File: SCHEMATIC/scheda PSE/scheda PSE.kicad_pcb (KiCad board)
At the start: 2 copper layers, 102.4 x 77.4 mm, 124 parts, among them J1 Debug, J2 Vin, J3 USB_B_Mini, J4 Vout 5V, J5 I2C_3V3, J6 UART0_3V3, Q1 IRLML0060TRPBF, Q2 PDTC114YT, Q3 IRLML9301, SW1 RESET_SW, SW2 PROG_SW, SW3 SW_U, SW4 SW_L, SW5 SW_R, SW6 SW_D, SW7 Power_button, U1 RP2040, U2 W25Q16JVUSSQ, U3 AT24C256, U4 oled_0.96"_128x64px, U5 TPS563201, U6 XC6705A331MR-G, U7 SAM-M8Q, U8 MMA8451Q, U9 TC1047A, Y1 12MHz

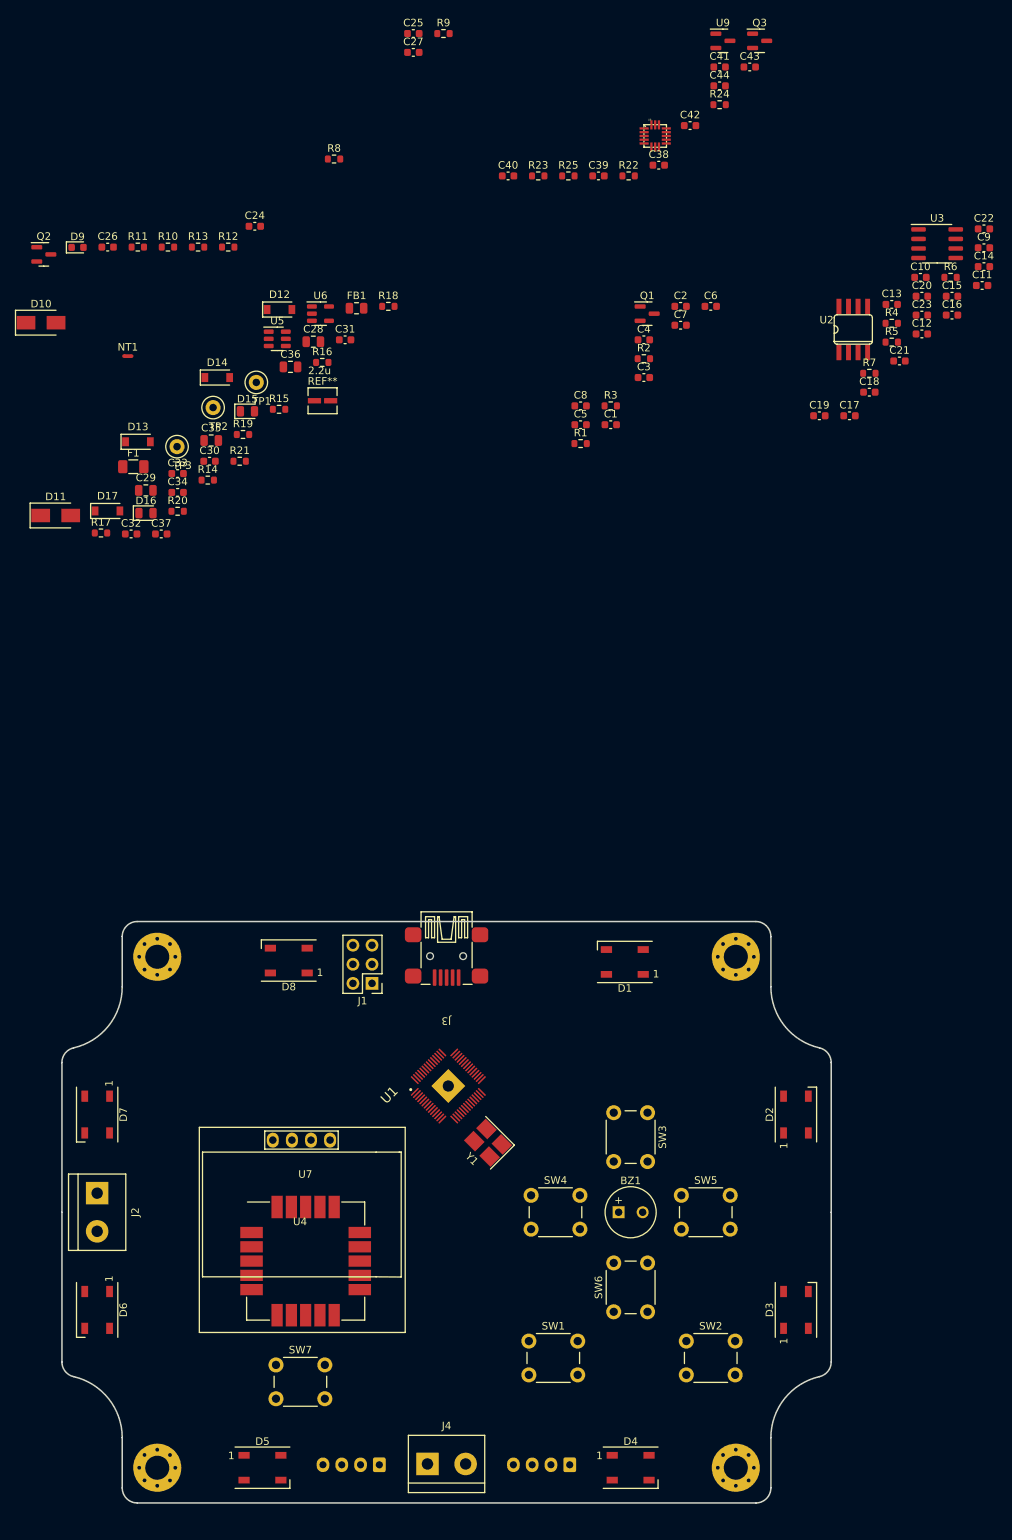
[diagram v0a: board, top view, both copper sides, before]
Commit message: Posizionati tutti i componenti
Posizionati tutti i componenti sulla scheda
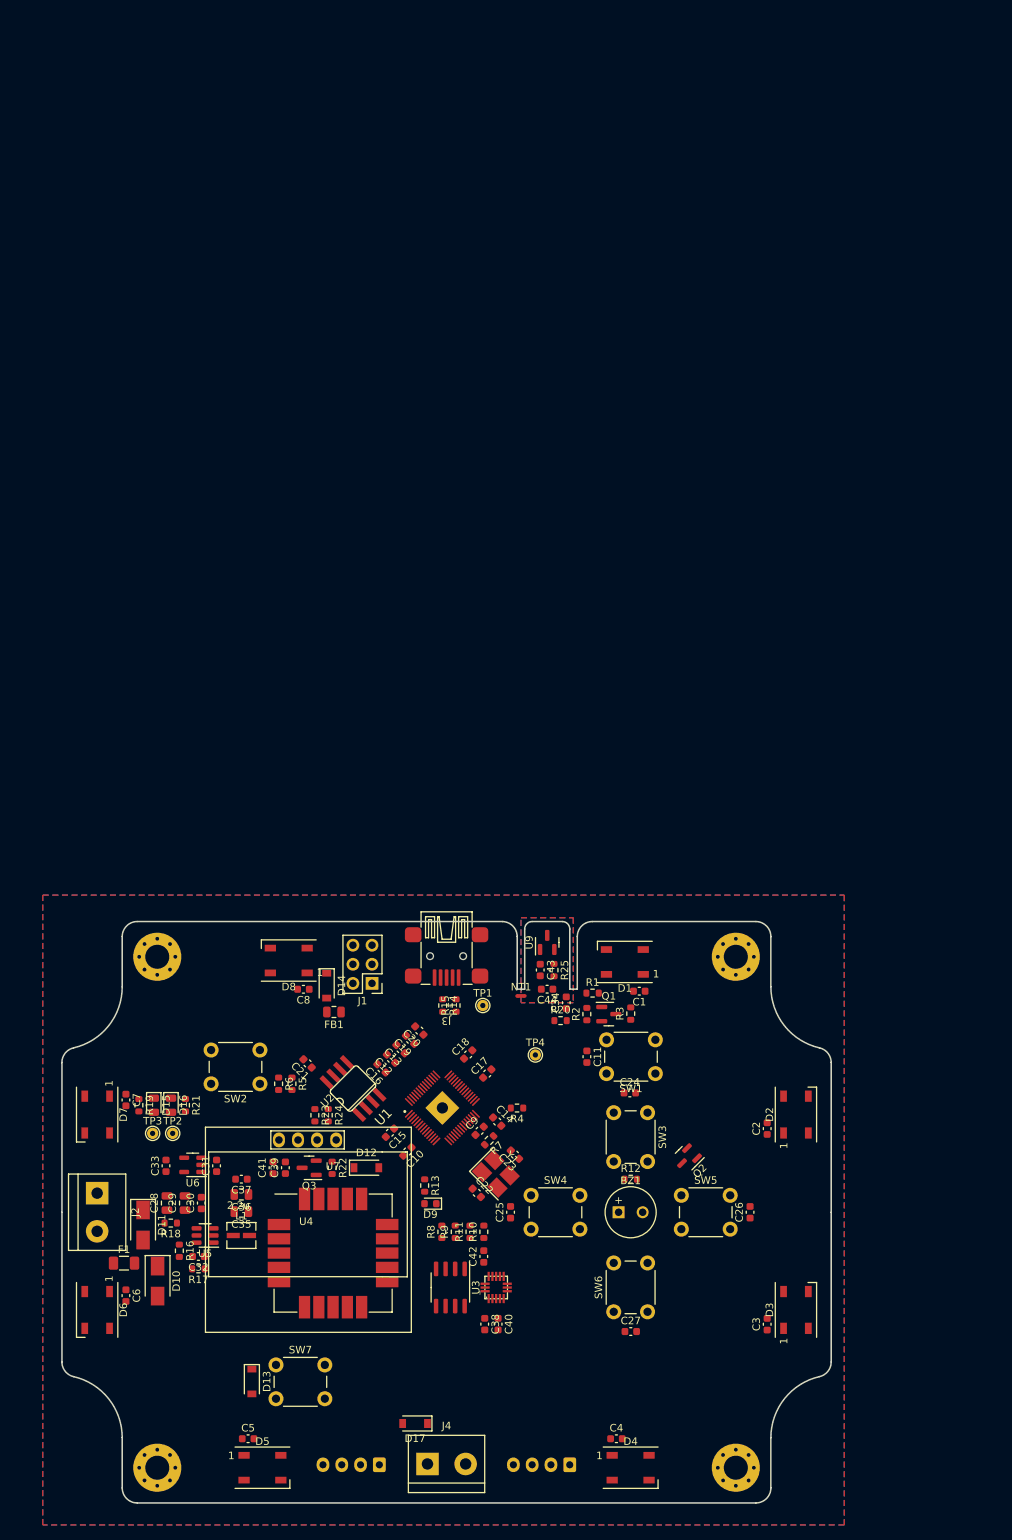
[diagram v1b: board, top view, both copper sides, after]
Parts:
- added TP2: 5V, TestPoint:TestPoint_THTPad_D1.5mm_Drill0.7mm, F.Cu at (119.1, 86.5)
- TP1: footprint TestPoint:TestPoint_Loop_D2.50mm_Drill1.0mm_LowProfile -> TestPoint:TestPoint_THTPad_D1.5mm_Drill0.7mm
- TP3: renamed from TP2; footprint TestPoint:TestPoint_Loop_D2.50mm_Drill1.0mm_LowProfile -> TestPoint:TestPoint_THTPad_D1.5mm_Drill0.7mm
- TP4: renamed from TP3; footprint TestPoint:TestPoint_Loop_D2.50mm_Drill1.0mm_LowProfile -> TestPoint:TestPoint_THTPad_D1.5mm_Drill0.7mm
- moved C27 172.7 mm to (180.0, 112.9)
- moved Q3 161.5 mm to (137.2, 91.1), turned to 180 degrees
- moved R9 159.5 mm to (156.7, 99.6), turned to 90 degrees
- moved C41 158.1 mm to (132.4, 91.1), turned to 90 degrees
- moved C25 157.4 mm to (164.0, 97.0), turned to 90 degrees
- moved C38 156.0 mm to (160.6, 111.9), turned to -90 degrees
- moved U8 154.7 mm to (162.1, 107.0), turned to 90 degrees
- moved C26 154.3 mm to (195.9, 97.0), turned to 90 degrees
- moved U3 153.3 mm to (156.0, 107.0), turned to -90 degrees
- moved C42 153.0 mm to (160.5, 102.9), turned to 90 degrees
- moved C6 152.9 mm to (112.8, 108.1), turned to -90 degrees
- moved C40 152.8 mm to (162.4, 111.9), turned to -90 degrees
- moved Q2 147.6 mm to (187.5, 89.8), turned to -135 degrees
- moved C4 146.3 mm to (178.1, 127.1)
- moved C22 145.0 mm to (159.5, 94.4), turned to -45 degrees
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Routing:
- added copper zone on B.Cu, net GND
- added copper zone on F.Cu, net GND
- added copper zone on B.Cu, net GNDA
- added copper zone on F.Cu, net GNDA
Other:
- outline, holes or cut-outs redrawn

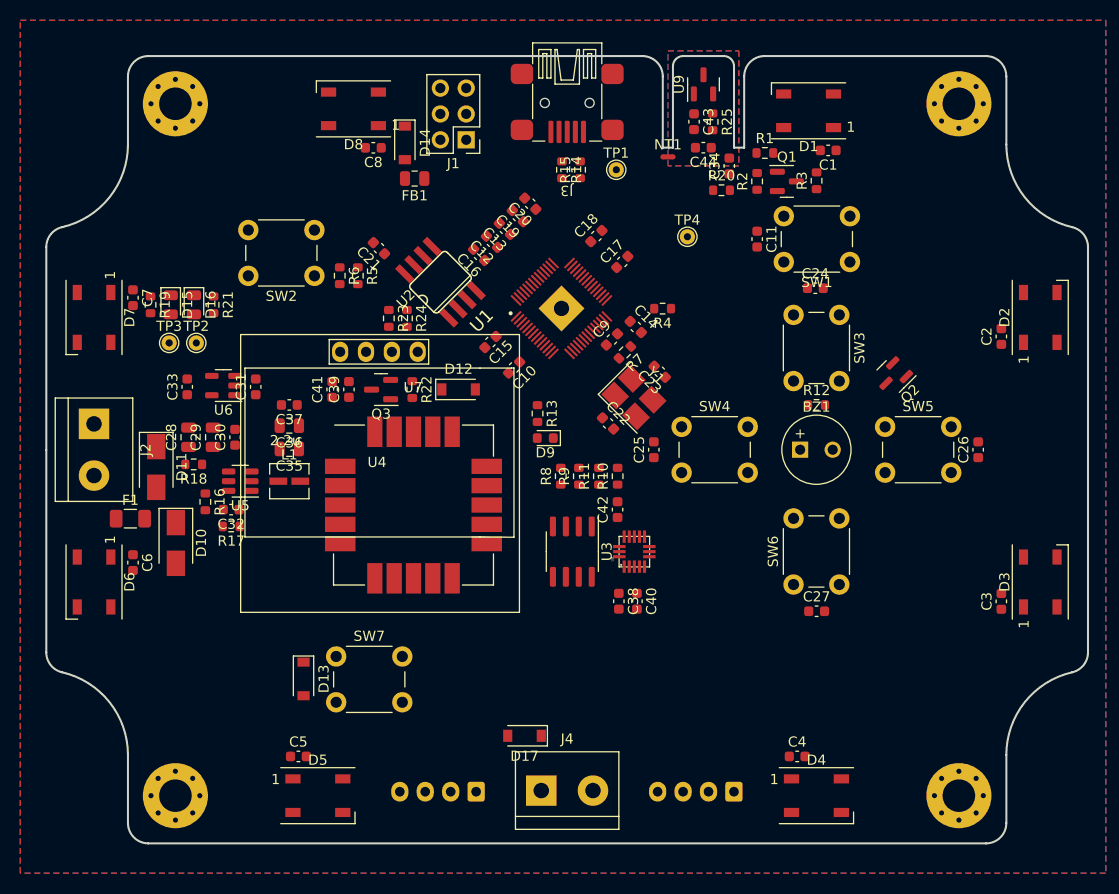
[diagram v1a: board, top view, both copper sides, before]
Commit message: iniziato lo broglio. Prima di continuare modificare pin schema
iniziato lo sbroglio della scheda, prima di continuare bisogna sistemare i pin che siano concordi con quelli degli altro (ovvero sistemarli come da tabella su telegram)
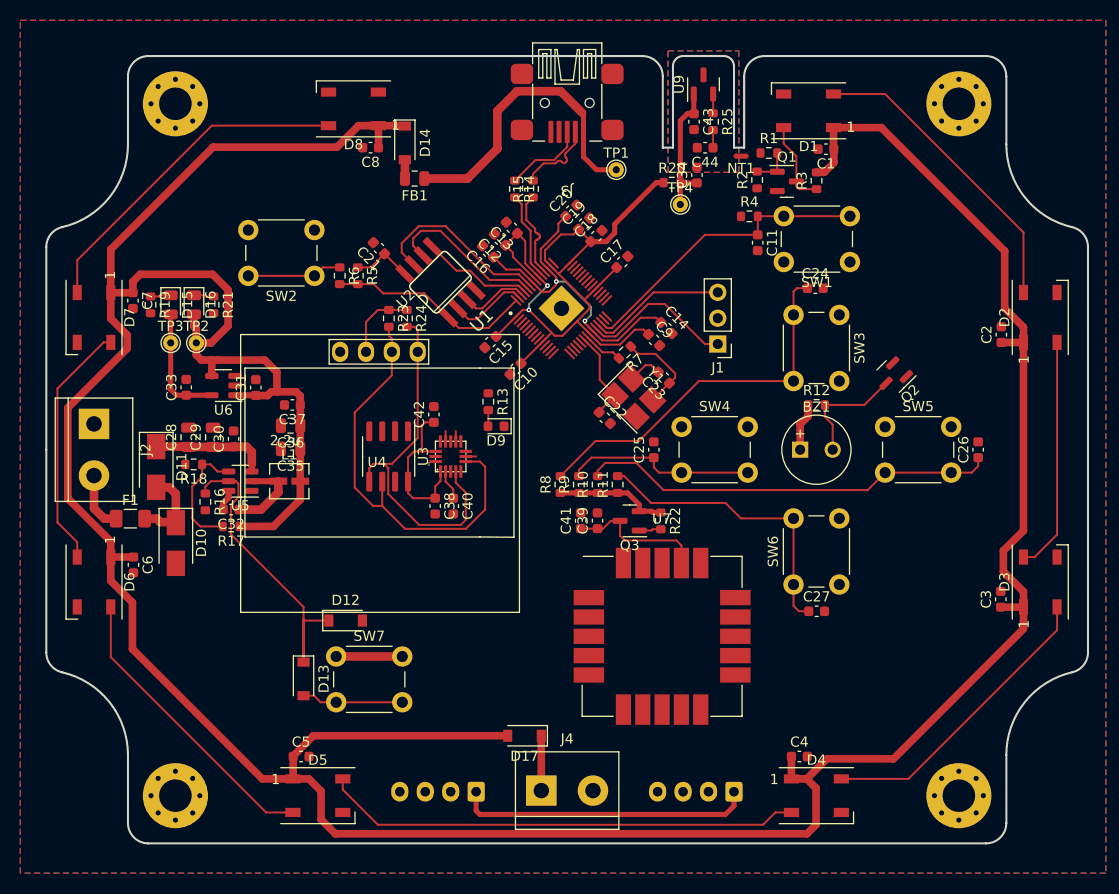
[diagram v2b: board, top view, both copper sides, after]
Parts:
- J1: value Debug -> Conn_01x03; footprint Connector_PinHeader_2.54mm:PinHeader_2x03_P2.54mm_Vertical -> Connector_PinHeader_2.54mm:PinHeader_1x03_P2.54mm_Vertical
- moved J1 31.8 mm to (170.3, 86.6)
- moved U7 27.6 mm to (165.1, 115.3)
- moved C41 27.6 mm to (156.8, 104.0)
- moved Q3 27.6 mm to (161.6, 104.0)
- moved R22 27.6 mm to (164.7, 104.0)
- moved C39 27.6 mm to (158.5, 104.0)
- moved D12 25.3 mm to (133.7, 113.8)
- moved C40 20.3 mm to (144.3, 102.5)
- moved C42 20.3 mm to (142.4, 93.5)
- moved C38 20.3 mm to (142.5, 102.5)
- moved U3 20.3 mm to (138.0, 97.7)
- moved U8 20.3 mm to (144.1, 97.7)
- moved R4 12.5 mm to (173.4, 74.1), turned to 0 degrees
- moved NT1 7.19 mm to (172.6, 68.1), turned to 180 degrees
- moved C19 6.56 mm to (157.2, 74.8), turned to 45 degrees
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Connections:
- net Net-(J3-Pad2) renamed /Alimentazione/D-
- net Net-(J3-Pad3) renamed /Alimentazione/D+
- C43 pad 1: +3V3 -> +3.3VA
- J1 pad 1: +3V3 -> /RP2040/SWCLK
- J1 pad 3: /RP2040/I2C1_SDA -> /RP2040/SWDIO
- J5 pad 1: +3.3V -> +3V3
- J6 pad 1: +3.3V -> +3V3
- R15 pad 1: /Alimentazione/USB_DM -> /Alimentazione/USB_DN
- U1 pad 29: /RP2040/I2C1_SDA -> unconnected-(U1-Pad29)
- U1 pad 30: /RP2040/I2C1_SCL -> unconnected-(U1-Pad30)
- U1 pad 46: /Alimentazione/USB_DP -> /Alimentazione/USB_DN
- U1 pad 47: /Alimentazione/USB_DM -> /Alimentazione/USB_DP
- U1 pad 54: /RP2040/FLASH_D2 -> /RP2040/~{FLASH_D2}
- U3 pad 8: +3.3V -> +3V3
- U9 pad 1: +3V3 -> +3.3VA
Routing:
- net +5V: track 0.00 -> 357.5 mm
- net +3V3: track 0.00 -> 155.1 mm, vias 0 -> 2
- net Net-(D4-Pad2): track 0.00 -> 47.1 mm
- net /I2C0_SCL: track 0.00 -> 41.4 mm
- net /Interfaccia utente/BUTTON_R: track 0.00 -> 41.2 mm
- net /Interfaccia utente/BUTTON_U: track 0.00 -> 37.1 mm
- net /I2C0_SDA: track 0.00 -> 36.8 mm
- net Net-(D7-Pad2): track 0.00 -> 33.4 mm
- net +1V1: track 0.00 -> 31.8 mm, vias 0 -> 2
- net /Alimentazione/BUCK_EN: track 0.00 -> 31.8 mm
- net /RP2040/RUN: track 0.00 -> 30.3 mm
- net /Alimentazione/VBUS: track 0.00 -> 30.2 mm
- net Net-(D1-Pad2): track 0.00 -> 30.2 mm
- net Net-(D3-Pad2): track 0.00 -> 29.5 mm
- net /Interfaccia utente/BUTTON_D: track 0.00 -> 29.3 mm
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
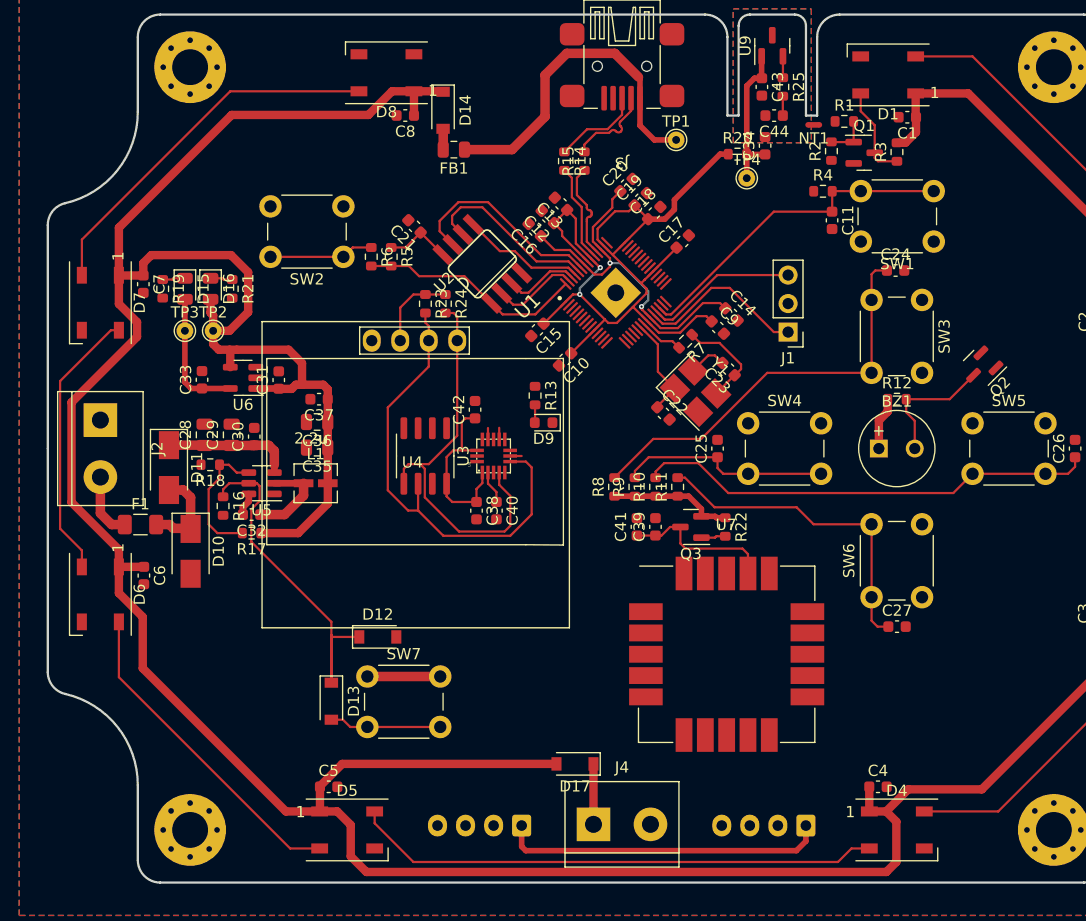
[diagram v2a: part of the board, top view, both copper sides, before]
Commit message: sistemato buzzer, e continuato lo sbroglio
sistemato il buzzer con un altro footprint e ho continuato lo sbroglio.
Teoricamente manca solo collegare i collegamenti tra le gpio del rp2040 e il resto dei componenti
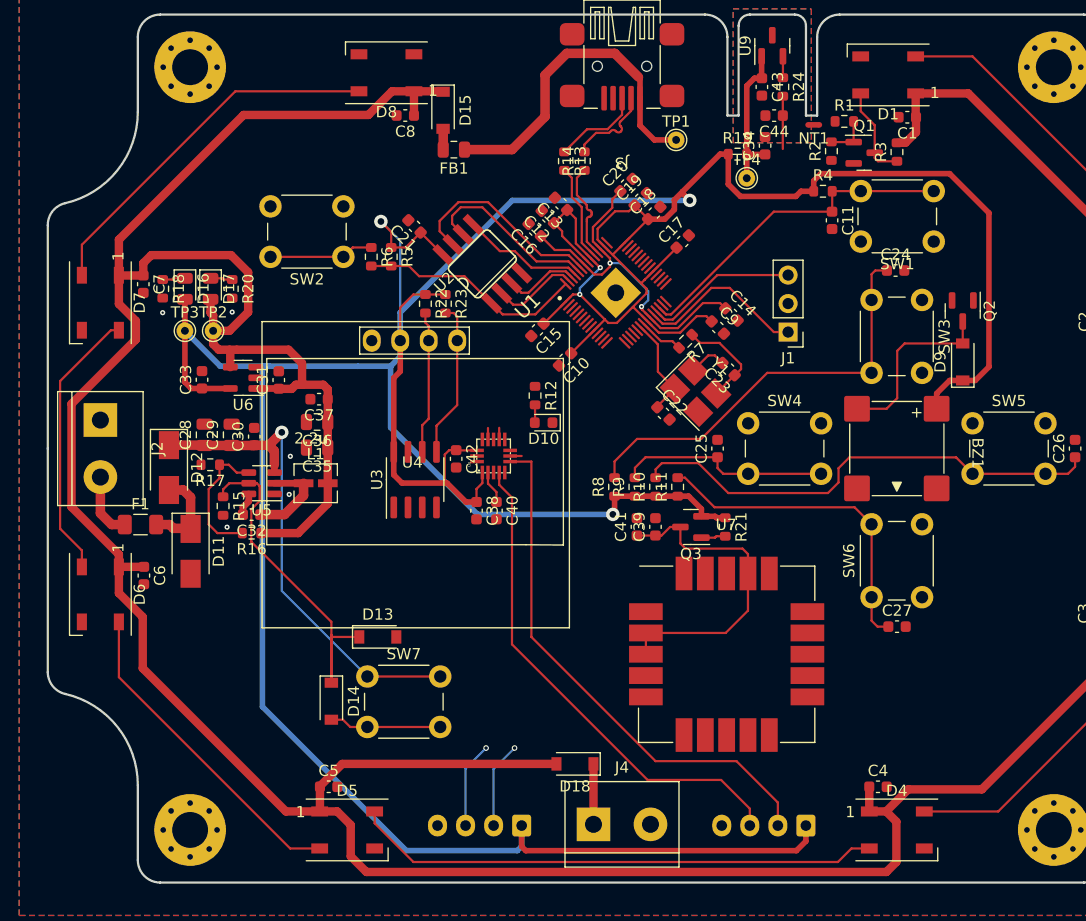
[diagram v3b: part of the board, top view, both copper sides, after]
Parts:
- removed the R12 at (180.0, 92.6)
- added D9: 1N4148, Diode_SMD:D_SOD-123, F.Cu at (185.9, 89.3)
- BZ1: footprint Buzzer_Beeper:MagneticBuzzer_Kingstate_KCG0601 -> _PSE:MLT-8530
- moved Q2 5.33 mm to (185.9, 84.7), turned to -90 degrees
- moved C42 4.70 mm to (140.7, 97.9), turned to -90 degrees
- moved U3 2.29 mm to (137.1, 99.8), turned to 90 degrees
- moved BZ1 1.60 mm to (180.0, 97.0), turned to -90 degrees
- renumbered D9 to D10, D10 to D11, D11 to D12, D12 to D13, D13 to D14, D14 to D15, D15 to D16, D16 to D17, D17 to D18, R13 to R12, R14 to R13, R15 to R14, R16 to R15, R17 to R16, R18 to R17, R19 to R18, R20 to R19, R21 to R20, R22 to R21, R23 to R22, R24 to R23, R25 to R24
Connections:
- BZ1 pad 1: +5V -> +3V3
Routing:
- net +3V3: track 155.1 -> 379.4 mm, vias 2 -> 5
- net +12V: track 18.0 -> 44.6 mm, vias 0 -> 1
- net /I2C0_SDA: track 36.8 -> 58.6 mm
- net /I2C0_SCL: track 41.4 -> 60.4 mm
- net Net-(C39-Pad1): track 13.8 -> 28.9 mm
- net /UART0_RX: track 0.00 -> 7.69 mm, vias 0 -> 1
- net /UART0_TX: track 0.00 -> 7.67 mm, vias 0 -> 1
- net +5V: track 357.5 -> 352.0 mm
- net Net-(BZ1-Pad2): track 11.6 -> 16.3 mm
- net /RP2040/TEMP_SENS: track 1.73 -> 4.71 mm
- net /Interfaccia utente/BUTTON_R: track 41.2 -> 43.2 mm
- net /Interfaccia utente/BUTTON_U: track 37.1 -> 37.9 mm
- net GND: vias 0 -> 5
